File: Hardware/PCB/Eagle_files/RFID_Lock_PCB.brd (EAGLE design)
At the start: 100 x 80 mm, 37 parts, among them IC1 74AHCT125, J3 Servo, K1 351, T2 2N2222

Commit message: Updated schematic
Updated board schematic to wire one relay pole to support a solenoid.  The second relay pole is left for general purpose use.
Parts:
- removed J4: (no value), SparkFun-Connectors:SCREWTERMINAL-3.5MM-3
- added D2: 1N4004, diode:DO41-10
- added SOLENOID: (no value), SparkFun-Connectors:SCREWTERMINAL-3.5MM-2
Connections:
- removed net N$24: J4.1, K1.O1
- removed net N$25: J4.3, K1.S1
- net GND: now also D2.A, SOLENOID.2
- net N$22: now also D2.C, K1.S1, SOLENOID.1; no longer J4.2, K1.P1
- net N$6: now also K1.P1
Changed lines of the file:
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@@
 <attribute name="VALUE" x="-88.392" y="-45.974" size="1.27" layer="27" ratio="10"/>
-</element>
-<element name="J4" library="SparkFun-Connectors" library_urn="urn:adsk.eagle:library:513" package="SCREWTERMINAL-3.5MM-3" package3d_urn="urn:adsk.eagle:package:38072/1" value="" x="-90.17" y="-52.07" smashed="yes">
-<attribute name="NAME" x="-88.011" y="-48.387" size="0.6096" layer="25" font="vector" ratio="20"/>
-<attribute name="PROD_ID" value="CONN-08288" x="-90.17" y="-52.07" size="1.778" layer="27" display="off"/>
-<attribute name="SF_ID" value="PRT-08235" x="-90.17" y="-52.07" size="1.778" layer="27" display="off"/>
-<attribute name="VALUE" x="-88.138" y="-56.642" size="0.6096" layer="27" font="vector" ratio="20"/>
 </element>
 <element name="J5" library="SparkFun-Connectors" library_urn="urn:adsk.eagle:library:513" package="SCREWTERMINAL-3.5MM-3" package3d_urn="urn:adsk.eagle:package:38072/1" value="" x="-90.17" y="-60.96" smashed="yes">
@@
 <attribute name="NAME" x="-98.171" y="-106.045" size="1.27" layer="25" ratio="10"/>
 <attribute name="VALUE" x="-97.155" y="-108.6358" size="1.27" layer="27" ratio="10"/>
+</element>
+<element name="SOLENOID" library="SparkFun-Connectors" library_urn="urn:adsk.eagle:library:513" package="SCREWTERMINAL-3.5MM-2" package3d_urn="urn:adsk.eagle:package:38050/1" value="" x="-97.79" y="-114.3" smashed="yes">
+<attribute name="NAME" x="-99.06" y="-111.76" size="0.6096" layer="25" font="vector" ratio="20"/>
+<attribute name="PROD_ID" value="CONN-08399" x="-97.79" y="-114.3" size="1.778" layer="27" display="off"/>
+<attribute name="VALUE" x="-99.06" y="-113.03" size="0.6096" layer="27" font="vector" ratio="20"/>
+</element>
+<element name="D2" library="diode" library_urn="urn:adsk.eagle:library:210" package="DO41-10" package3d_urn="urn:adsk.eagle:package:43336/1" value="1N4004" x="-93.98" y="-121.92" smashed="yes">
+<attribute name="NAME" x="-96.012" y="-120.269" size="1.27" layer="25" ratio="10"/>
+<attribute name="VALUE" x="-96.012" y="-124.714" size="1.27" layer="27" ratio="10"/>
 </element>
 </elements>
@@
 <contactref element="R7" pad="1"/>
 <contactref element="R8" pad="1"/>
+<contactref element="SOLENOID" pad="2"/>
+<contactref element="D2" pad="A"/>
+<wire x1="-94.29" y1="-114.3" x2="-88.9" y2="-121.92" width="0" layer="19" extent="1-1"/>
+<wire x1="-100.33" y1="-107.95" x2="-94.29" y2="-114.3" width="0" layer="19" extent="1-1"/>
 <wire x1="-100.33" y1="-101.6" x2="-100.33" y2="-107.95" width="0" layer="19" extent="1-1"/>
 <wire x1="-90.79" y1="-93.98" x2="-100.33" y2="-101.6" width="0" layer="19" extent="1-1"/>
@@
 <contactref element="MOT_PWR" pad="1"/>
 <contactref element="C9" pad="1"/>
-<wire x1="-59.69" y1="-17.78" x2="-96.52" y2="-59.69" width="0" layer="19" extent="1-1"/>
+<contactref element="K1" pad="P1"/>
+<wire x1="-83.82" y1="-36.83" x2="-96.52" y2="-59.69" width="0" layer="19" extent="1-1"/>
+<wire x1="-59.69" y1="-17.78" x2="-83.82" y2="-36.83" width="0" layer="19" extent="1-1"/>
 <wire x1="-52.07" y1="-3.81" x2="-59.69" y2="-17.78" width="0" layer="19" extent="1-1"/>
 <wire x1="-53.34" y1="57.15" x2="-52.07" y2="-3.81" width="0" layer="19" extent="1-1"/>
@@
 <wire x1="-87.63" y1="-22.86" x2="-91.44" y2="-29.21" width="0" layer="19" extent="1-1"/>
 </signal>
-<signal name="N$22">
-<contactref element="K1" pad="P1"/>
-<contactref element="J4" pad="2"/>
-<wire x1="-83.82" y1="-36.83" x2="-86.67" y2="-52.07" width="0" layer="19" extent="1-1"/>
-</signal>
-<signal name="N$24">
-<contactref element="K1" pad="O1"/>
-<contactref element="J4" pad="1"/>
-<wire x1="-78.74" y1="-36.83" x2="-90.17" y2="-52.07" width="0" layer="19" extent="1-1"/>
-</signal>
-<signal name="N$25">
-<contactref element="K1" pad="S1"/>
-<contactref element="J4" pad="3"/>
-<wire x1="-73.66" y1="-36.83" x2="-83.17" y2="-52.07" width="0" layer="19" extent="1-1"/>
-</signal>
 <signal name="N$26">
 <contactref element="K1" pad="P2"/>
@@
 <wire x1="-73.66" y1="-29.21" x2="-83.17" y2="-60.96" width="0" layer="19" extent="1-1"/>
 </signal>
+<signal name="N$22">
+<contactref element="SOLENOID" pad="1"/>
+<contactref element="K1" pad="S1"/>
+<contactref element="D2" pad="C"/>
+<wire x1="-97.79" y1="-114.3" x2="-99.06" y2="-121.92" width="0" layer="19" extent="1-1"/>
+<wire x1="-73.66" y1="-36.83" x2="-97.79" y2="-114.3" width="0" layer="19" extent="1-1"/>
+</signal>
 </signals>

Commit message: Placed parts on PCB
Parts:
- moved D2 202.4 mm to (57.1, 12.7)
- moved LED 199.0 mm to (68.6, 33.0), turned to 90 degrees
- moved SOLENOID 193.8 mm to (55.9, 3.81)
- moved SENSOR2 185.3 mm to (3.81, 69.8), turned to 270 degrees
- moved DOOR 183.5 mm to (68.6, 8.89), turned to 90 degrees
- moved SENSOR1 182.1 mm to (3.81, 57.1), turned to 270 degrees
- moved R8 174.4 mm to (22.9, 21.6), turned to 90 degrees
- moved R7 173.3 mm to (27.9, 21.6), turned to 90 degrees
- moved T2 165.2 mm to (68.6, 24.1), turned to 270 degrees
- moved D1 160.8 mm to (59.7, 24.1), turned to 270 degrees
- moved J5 147.1 mm to (41.9, 3.81)
- moved K1 146.9 mm to (48.3, 22.9), turned to 180 degrees
- moved C9 142.6 mm to (29.2, 5.08)
- moved R2 140.9 mm to (57.1, 38.1), turned to 270 degrees
- moved SP1 132.3 mm to (48.3, 45.7)
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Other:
- board size 100 x 80 mm -> 72.1 x 76.2 mm

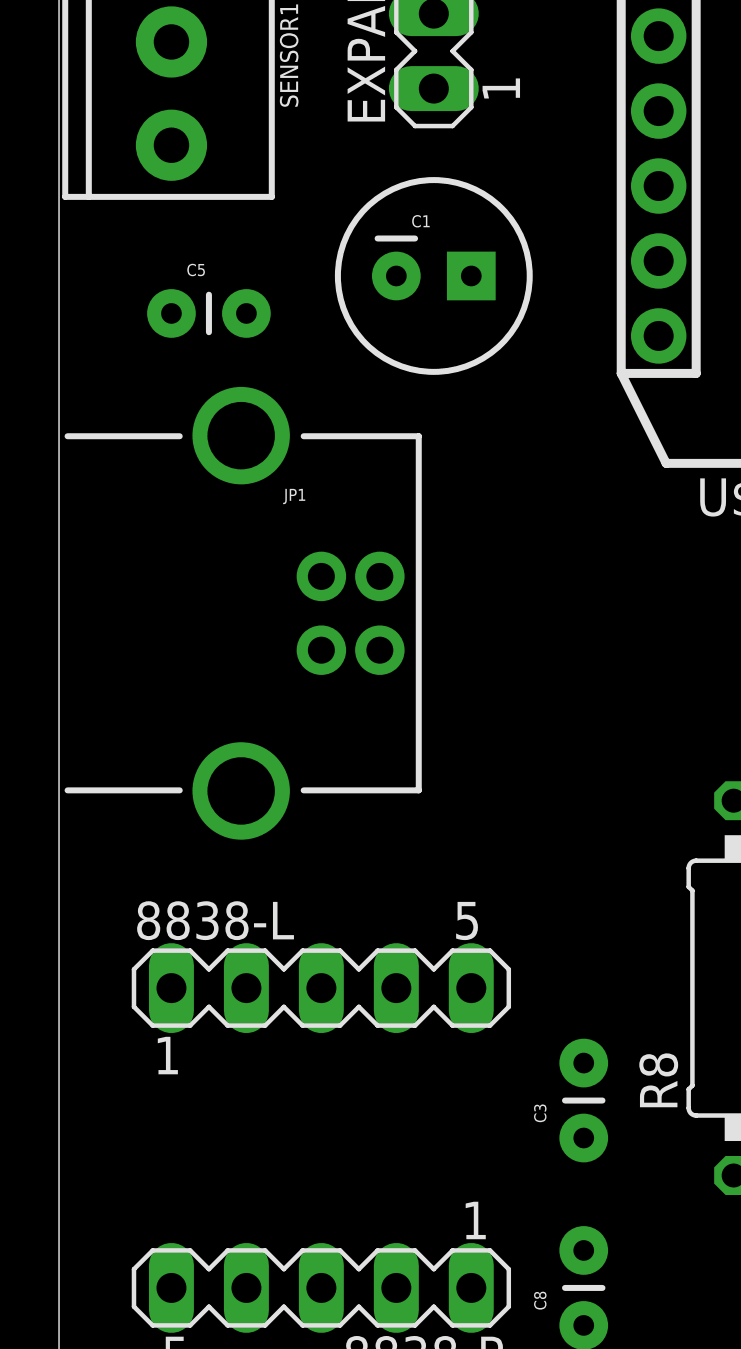
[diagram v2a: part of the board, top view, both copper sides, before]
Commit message: Corrected PCB
Corrected pin header spacing for motor driver.
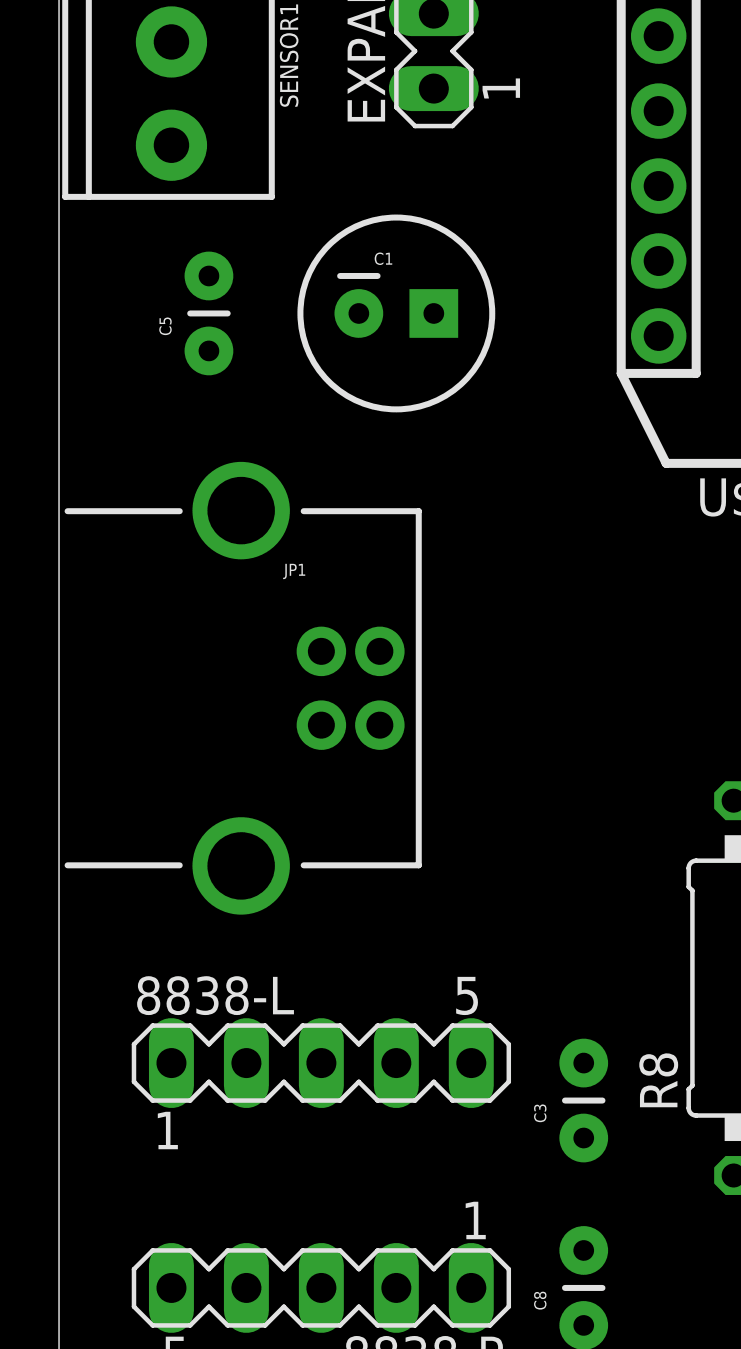
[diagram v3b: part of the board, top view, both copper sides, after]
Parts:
- moved 8838-L 2.54 mm to (8.89, 19.1)
- moved JP1 2.54 mm to (8.89, 31.8)
- moved C5 1.80 mm to (5.08, 43.2), turned to 90 degrees
- moved C1 1.80 mm to (11.4, 44.5)
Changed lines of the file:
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@@
 </autorouter>
 <elements>
-<element name="8838-L" library="con-lstb" library_urn="urn:adsk.eagle:library:162" package="MA05-1" package3d_urn="urn:adsk.eagle:package:8332/1" value="" x="8.89" y="21.59" smashed="yes">
-<attribute name="MF" value="" x="50.8" y="-35.56" size="1.778" layer="27" display="off"/>
-<attribute name="MPN" value="" x="50.8" y="-35.56" size="1.778" layer="27" display="off"/>
-<attribute name="NAME" x="2.54" y="23.241" size="1.27" layer="25" ratio="10"/>
-<attribute name="OC_FARNELL" value="unknown" x="50.8" y="-35.56" size="1.778" layer="27" display="off"/>
-<attribute name="OC_NEWARK" value="unknown" x="50.8" y="-35.56" size="1.778" layer="27" display="off"/>
-<attribute name="VALUE" x="6.35" y="18.669" size="1.27" layer="27" ratio="10"/>
+<element name="8838-L" library="con-lstb" library_urn="urn:adsk.eagle:library:162" package="MA05-1" package3d_urn="urn:adsk.eagle:package:8332/1" value="" x="8.89" y="19.05" smashed="yes">
+<attribute name="MF" value="" x="50.8" y="-38.1" size="1.778" layer="27" display="off"/>
+<attribute name="MPN" value="" x="50.8" y="-38.1" size="1.778" layer="27" display="off"/>
+<attribute name="NAME" x="2.54" y="20.701" size="1.27" layer="25" ratio="10"/>
+<attribute name="OC_FARNELL" value="unknown" x="50.8" y="-38.1" size="1.778" layer="27" display="off"/>
+<attribute name="OC_NEWARK" value="unknown" x="50.8" y="-38.1" size="1.778" layer="27" display="off"/>
+<attribute name="VALUE" x="6.35" y="16.129" size="1.27" layer="27" ratio="10"/>
 </element>
 <element name="8838-R" library="con-lstb" library_urn="urn:adsk.eagle:library:162" package="MA05-1" package3d_urn="urn:adsk.eagle:package:8332/1" value="" x="8.89" y="11.43" smashed="yes" rot="R180">
@@
 <attribute name="VALUE" x="11.43" y="14.351" size="1.27" layer="27" ratio="10" rot="R180"/>
 </element>
-<element name="C1" library="SparkFun-Capacitors" package="CPOL-RADIAL-100UF-25V" value="100uf" x="12.7" y="45.72" smashed="yes">
-<attribute name="NAME" x="11.938" y="47.371" size="0.4064" layer="25"/>
-<attribute name="VALUE" x="10.795" y="41.402" size="0.8128" layer="27"/>
+<element name="C1" library="SparkFun-Capacitors" package="CPOL-RADIAL-100UF-25V" value="100uf" x="11.43" y="44.45" smashed="yes">
+<attribute name="NAME" x="10.668" y="46.101" size="0.4064" layer="25"/>
+<attribute name="VALUE" x="9.525" y="40.132" size="0.8128" layer="27"/>
 </element>
 <element name="C2" library="SparkFun-Passives" package="CAP-PTH-SMALL" value="0.1 uF" x="66.04" y="17.78" smashed="yes">
@@
 <attribute name="VALUE" x="47.244" y="53.086" size="0.4064" layer="27"/>
 </element>
-<element name="C5" library="SparkFun-Passives" package="CAP-PTH-SMALL" value="0.1 uF" x="3.81" y="44.45" smashed="yes">
-<attribute name="NAME" x="4.318" y="45.72" size="0.4064" layer="25"/>
-<attribute name="VALUE" x="4.064" y="42.926" size="0.4064" layer="27"/>
+<element name="C5" library="SparkFun-Passives" package="CAP-PTH-SMALL" value="0.1 uF" x="5.08" y="43.18" smashed="yes" rot="R90">
+<attribute name="NAME" x="3.81" y="43.688" size="0.4064" layer="25" rot="R90"/>
+<attribute name="VALUE" x="6.604" y="43.434" size="0.4064" layer="27" rot="R90"/>
 </element>
 <element name="C6" library="SparkFun-Passives" package="CAP-PTH-SMALL" value="0.1 uF" x="60.96" y="48.26" smashed="yes" rot="R90">
@@
 <attribute name="VALUE" x="71.501" y="43.18" size="1.27" layer="27" ratio="10" rot="R90"/>
 </element>
-<element name="JP1" library="SparkFun-Connectors" package="USB-B-PTH" value="USB-B" x="8.89" y="34.29" smashed="yes">
-<attribute name="NAME" x="7.62" y="38.1" size="0.4064" layer="25"/>
-<attribute name="PROD_ID" value="CONN-08278" x="53.34" y="25.4" size="1.778" layer="27" display="off"/>
-<attribute name="VALUE" x="7.62" y="36.83" size="0.4064" layer="27"/>
+<element name="JP1" library="SparkFun-Connectors" package="USB-B-PTH" value="USB-B" x="8.89" y="31.75" smashed="yes">
+<attribute name="NAME" x="7.62" y="35.56" size="0.4064" layer="25"/>
+<attribute name="PROD_ID" value="CONN-08278" x="53.34" y="22.86" size="1.778" layer="27" display="off"/>
+<attribute name="VALUE" x="7.62" y="34.29" size="0.4064" layer="27"/>
 </element>
 <element name="R1" library="rcl" package="0309/12" value="470 ohm" x="62.23" y="38.1" smashed="yes" rot="R270">
@@
 <wire x1="21.28" y1="3.81" x2="45.974" y2="45.72" width="0" layer="19" extent="1-1"/>
 <wire x1="39.37" y1="11.43" x2="21.28" y2="3.81" width="0" layer="19" extent="1-1"/>
-<wire x1="8.89" y1="33.04" x2="39.37" y2="11.43" width="0" layer="19" extent="1-1"/>
-<wire x1="20.32" y1="69.088" x2="8.89" y2="33.04" width="0" layer="19" extent="1-1"/>
+<wire x1="8.89" y1="30.5" x2="39.37" y2="11.43" width="0" layer="19" extent="1-1"/>
+<wire x1="20.32" y1="69.088" x2="8.89" y2="30.5" width="0" layer="19" extent="1-1"/>
 <wire x1="44.45" y1="73.66" x2="20.32" y2="69.088" width="0" layer="19" extent="1-1"/>
 <wire x1="44.45" y1="66.04" x2="44.45" y2="73.66" width="0" layer="19" extent="1-1"/>
@@
 <wire x1="17.78" y1="19.05" x2="68.58" y2="17.78" width="0" layer="19" extent="1-1"/>
 <wire x1="49.53" y1="54.61" x2="17.78" y2="19.05" width="0" layer="19" extent="1-1"/>
-<wire x1="6.35" y1="44.45" x2="49.53" y2="54.61" width="0" layer="19" extent="1-1"/>
-<wire x1="60.96" y1="50.8" x2="6.35" y2="44.45" width="0" layer="19" extent="1-1"/>
+<wire x1="5.08" y1="45.72" x2="49.53" y2="54.61" width="0" layer="19" extent="1-1"/>
+<wire x1="60.96" y1="50.8" x2="5.08" y2="45.72" width="0" layer="19" extent="1-1"/>
 <wire x1="12.7" y1="73.66" x2="60.96" y2="50.8" width="0" layer="19" extent="1-1"/>
 <wire x1="17.78" y1="12.7" x2="12.7" y2="73.66" width="0" layer="19" extent="1-1"/>
 <wire x1="69.85" y1="60.96" x2="12.7" y2="73.66" width="0" layer="19" extent="1-1"/>
-<wire x1="11.43" y1="45.72" x2="44.45" y2="73.66" width="0" layer="19" extent="1-1"/>
-<wire x1="3.81" y1="21.59" x2="11.43" y2="45.72" width="0" layer="19" extent="1-1"/>
-<wire x1="3.81" y1="11.43" x2="3.81" y2="21.59" width="0" layer="19" extent="1-1"/>
+<wire x1="10.16" y1="44.45" x2="44.45" y2="73.66" width="0" layer="19" extent="1-1"/>
+<wire x1="3.81" y1="19.05" x2="10.16" y2="44.45" width="0" layer="19" extent="1-1"/>
+<wire x1="3.81" y1="11.43" x2="3.81" y2="19.05" width="0" layer="19" extent="1-1"/>
 <wire x1="69.85" y1="71.12" x2="69.85" y2="66.04" width="0" layer="19" extent="1-1"/>
 <wire x1="38.1" y1="64.008" x2="44.45" y2="66.04" width="0" layer="19" extent="1-1"/>
@@
 <wire x1="52.07" y1="26.67" x2="59.69" y2="29.21" width="0" layer="19" extent="1-1"/>
 <wire x1="36.83" y1="11.43" x2="52.07" y2="26.67" width="0" layer="19" extent="1-1"/>
-<wire x1="10.8712" y1="33.04" x2="36.83" y2="11.43" width="0" layer="19" extent="1-1"/>
-<wire x1="20.32" y1="71.628" x2="10.8712" y2="33.04" width="0" layer="19" extent="1-1"/>
-<wire x1="13.97" y1="45.72" x2="20.32" y2="71.628" width="0" layer="19" extent="1-1"/>
-<wire x1="52.07" y1="73.66" x2="13.97" y2="45.72" width="0" layer="19" extent="1-1"/>
+<wire x1="10.8712" y1="30.5" x2="36.83" y2="11.43" width="0" layer="19" extent="1-1"/>
+<wire x1="20.32" y1="71.628" x2="10.8712" y2="30.5" width="0" layer="19" extent="1-1"/>
+<wire x1="12.7" y1="44.45" x2="20.32" y2="71.628" width="0" layer="19" extent="1-1"/>
+<wire x1="52.07" y1="73.66" x2="12.7" y2="44.45" width="0" layer="19" extent="1-1"/>
 <wire x1="12.7" y1="67.31" x2="52.07" y2="73.66" width="0" layer="19" extent="1-1"/>
 <wire x1="12.7" y1="69.85" x2="12.7" y2="67.31" width="0" layer="19" extent="1-1"/>
 <wire x1="68.58" y1="46.99" x2="52.07" y2="73.66" width="0" layer="19" extent="1-1"/>
 <wire x1="46.99" y1="54.61" x2="68.58" y2="46.99" width="0" layer="19" extent="1-1"/>
-<wire x1="3.81" y1="44.45" x2="46.99" y2="54.61" width="0" layer="19" extent="1-1"/>
-<wire x1="60.96" y1="48.26" x2="3.81" y2="44.45" width="0" layer="19" extent="1-1"/>
+<wire x1="5.08" y1="43.18" x2="46.99" y2="54.61" width="0" layer="19" extent="1-1"/>
+<wire x1="60.96" y1="48.26" x2="5.08" y2="43.18" width="0" layer="19" extent="1-1"/>
 <wire x1="66.04" y1="17.78" x2="46.99" y2="54.61" width="0" layer="19" extent="1-1"/>
 </signal>
@@
 <wire x1="38.1" y1="71.628" x2="3.81" y2="66.35" width="0" layer="19" extent="1-1"/>
 <wire x1="12.7" y1="64.77" x2="38.1" y2="71.628" width="0" layer="19" extent="1-1"/>
-<wire x1="6.35" y1="21.59" x2="12.7" y2="64.77" width="0" layer="19" extent="1-1"/>
-<wire x1="17.78" y1="16.51" x2="6.35" y2="21.59" width="0" layer="19" extent="1-1"/>
+<wire x1="6.35" y1="19.05" x2="12.7" y2="64.77" width="0" layer="19" extent="1-1"/>
+<wire x1="17.78" y1="16.51" x2="6.35" y2="19.05" width="0" layer="19" extent="1-1"/>
 <wire x1="15.24" y1="73.66" x2="17.78" y2="16.51" width="0" layer="19" extent="1-1"/>
 <wire x1="17.78" y1="10.16" x2="15.24" y2="73.66" width="0" layer="19" extent="1-1"/>
@@
 <contactref element="R7" pad="2"/>
 <wire x1="38.1" y1="48.768" x2="27.94" y2="27.94" width="0" layer="19" extent="1-1"/>
-<wire x1="11.43" y1="21.59" x2="38.1" y2="48.768" width="0" layer="19" extent="1-1"/>
+<wire x1="11.43" y1="19.05" x2="38.1" y2="48.768" width="0" layer="19" extent="1-1"/>
 </signal>
 <signal name="N$5">
@@
 <contactref element="R8" pad="2"/>
 <wire x1="38.1" y1="51.308" x2="22.86" y2="27.94" width="0" layer="19" extent="1-1"/>
-<wire x1="8.89" y1="21.59" x2="38.1" y2="51.308" width="0" layer="19" extent="1-1"/>
+<wire x1="8.89" y1="19.05" x2="38.1" y2="51.308" width="0" layer="19" extent="1-1"/>
 </signal>
 <signal name="N$6">
